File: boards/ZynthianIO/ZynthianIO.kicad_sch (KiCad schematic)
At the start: 25 parts, among them J1 Raspberry_Pi_2_3, J2 GPIO, U1 MCP23017_SP, U2 6N138, U3 74LS14

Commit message: Added IO Expander 3D model and connectors to case design, added references to sources.
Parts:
- Ctrl1, Ctrl2, Ctrl3, Ctrl4: footprint Connector_PinSocket_2.54mm:PinSocket_1x04_P2.54mm_Vertical -> Connector_PinHeader_2.54mm:PinHeader_1x04_P2.54mm_Vertical
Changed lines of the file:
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@@
       (effects (font (size 1.27 1.27)) (justify left))
     )
-    (property "Footprint" "Connector_PinSocket_2.54mm:PinSocket_1x04_P2.54mm_Vertical" (at 130.81 173.99 0)
+    (property "Footprint" "Connector_PinHeader_2.54mm:PinHeader_1x04_P2.54mm_Vertical" (at 130.81 173.99 0)
       (effects (font (size 1.27 1.27)) hide)
     )
@@
       (effects (font (size 1.27 1.27)) (justify left))
     )
-    (property "Footprint" "Connector_PinSocket_2.54mm:PinSocket_1x04_P2.54mm_Vertical" (at 130.81 158.75 0)
+    (property "Footprint" "Connector_PinHeader_2.54mm:PinHeader_1x04_P2.54mm_Vertical" (at 130.81 158.75 0)
       (effects (font (size 1.27 1.27)) hide)
     )
@@
       (effects (font (size 1.27 1.27)) (justify left))
     )
-    (property "Footprint" "Connector_PinSocket_2.54mm:PinSocket_1x04_P2.54mm_Vertical" (at 130.81 128.27 0)
+    (property "Footprint" "Connector_PinHeader_2.54mm:PinHeader_1x04_P2.54mm_Vertical" (at 130.81 128.27 0)
       (effects (font (size 1.27 1.27)) hide)
     )
@@
       (effects (font (size 1.27 1.27)) (justify left))
     )
-    (property "Footprint" "Connector_PinSocket_2.54mm:PinSocket_1x04_P2.54mm_Vertical" (at 130.81 143.51 0)
-      (effects (font (size 1.27 1.27)) hide)
-    )
+    (property "Footprint" "Connector_PinHeader_2.54mm:PinHeader_1x04_P2.54mm_Vertical" (at 130.81 143.51 0)
+      (effects (font (size 1.27 1.27)) hide)
+    )

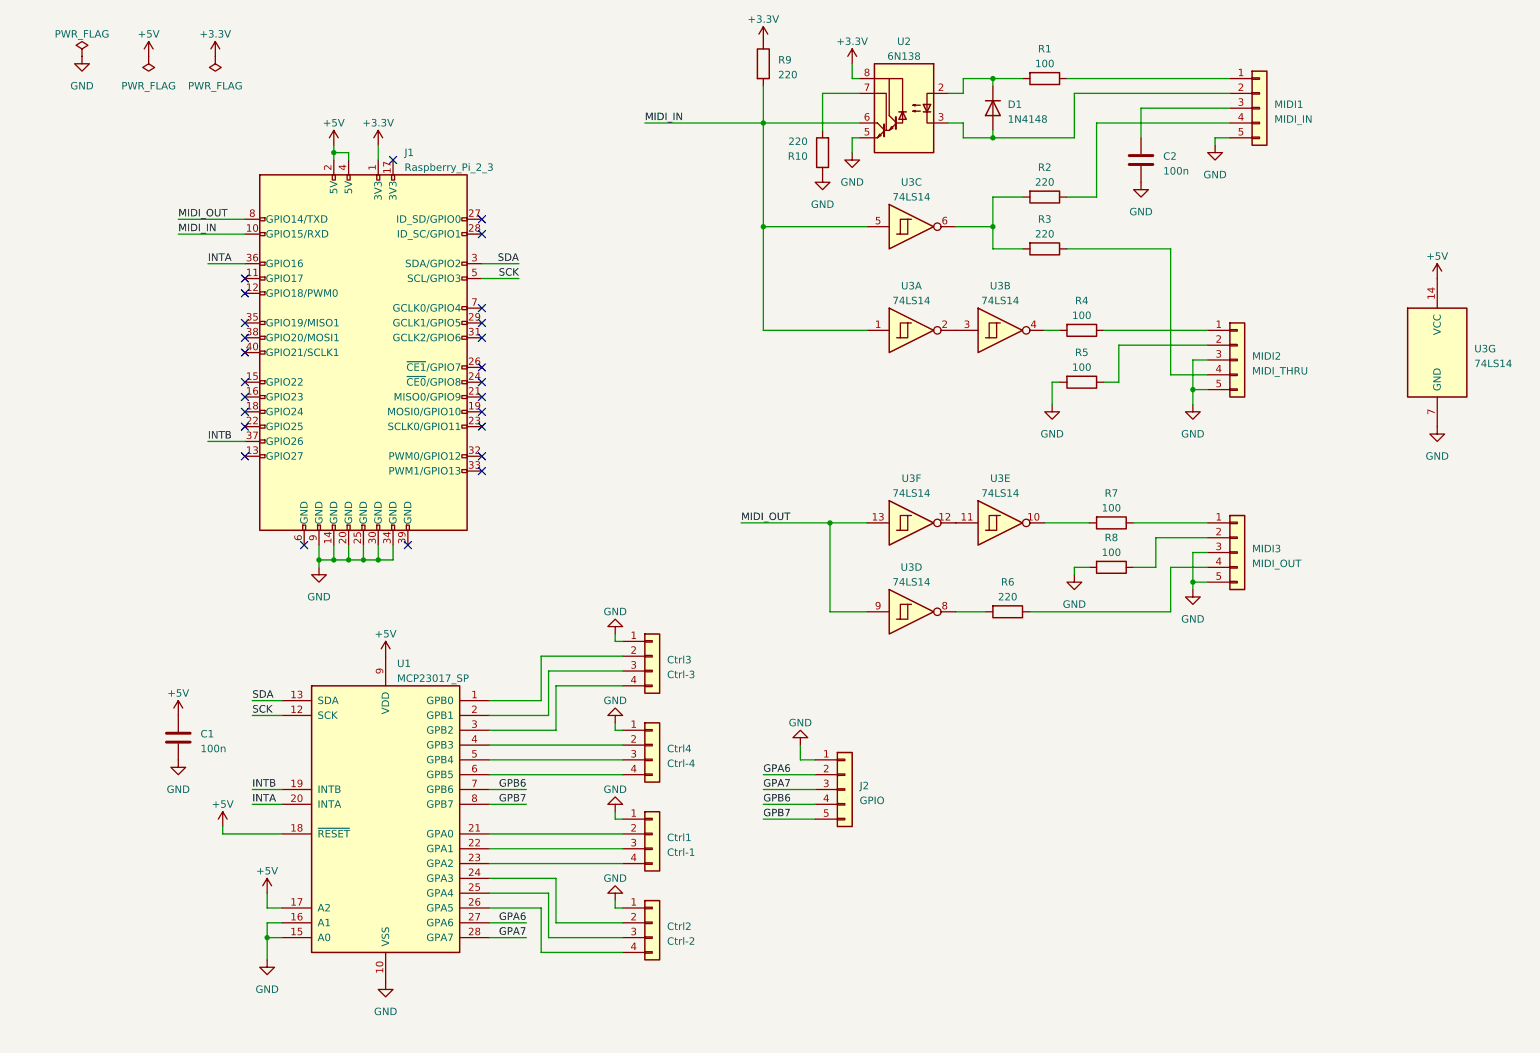
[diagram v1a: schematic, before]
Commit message: Updated IO expander board with Raspberry HAT template PCB design
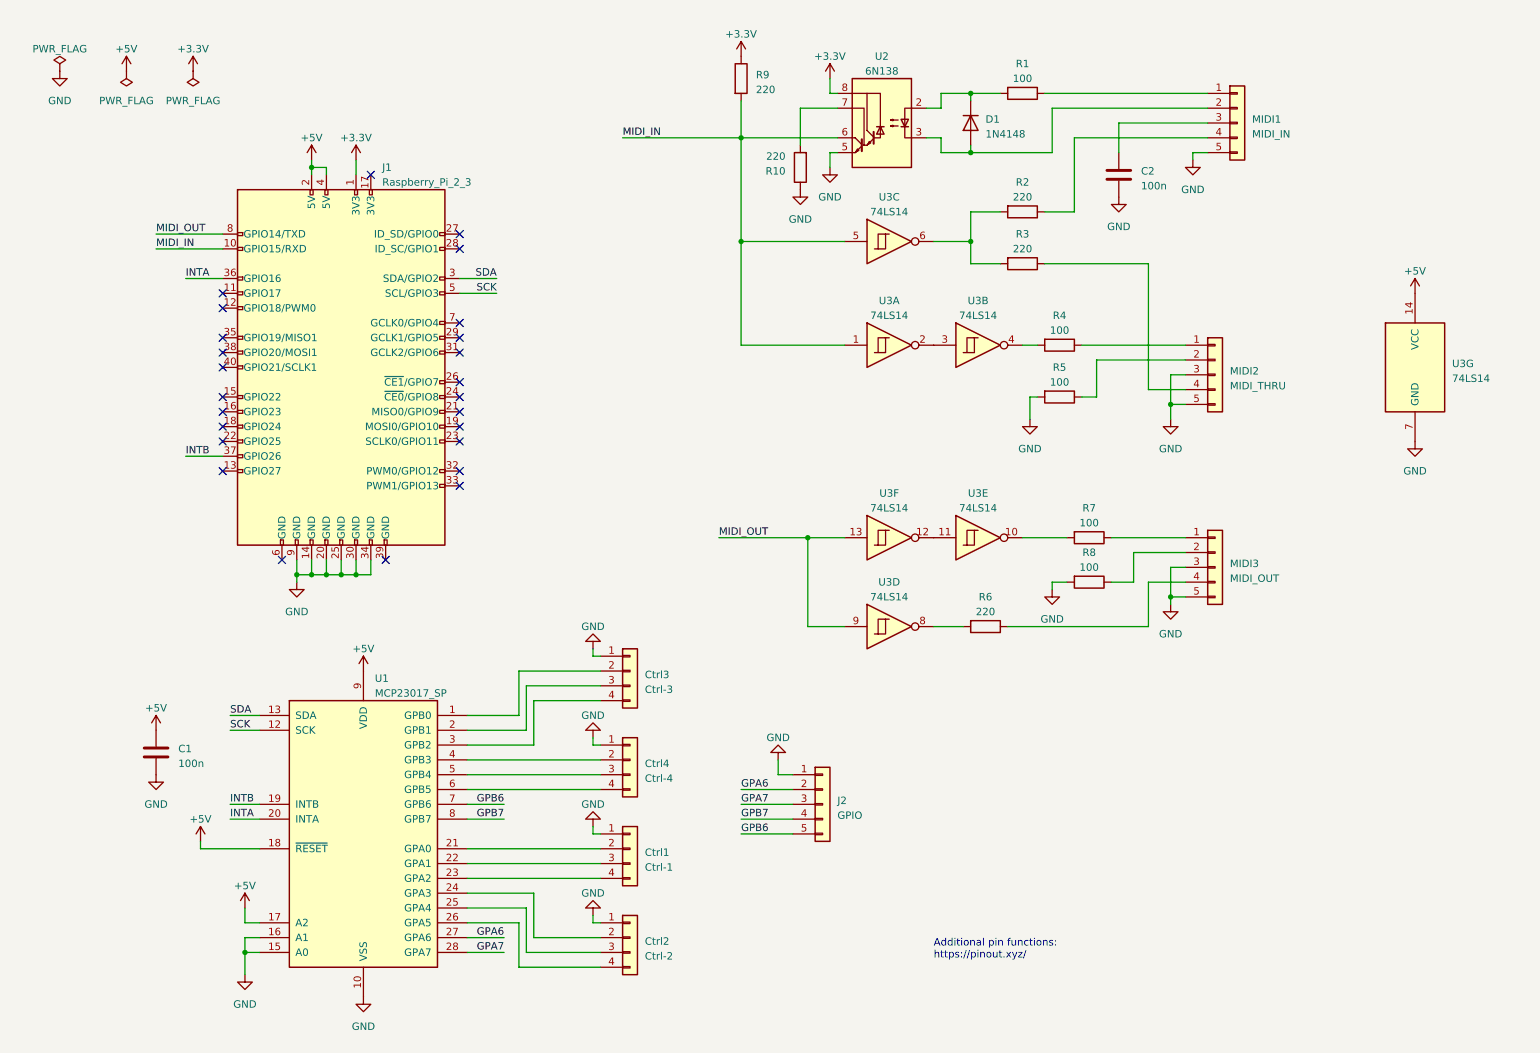
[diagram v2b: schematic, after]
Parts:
- R1, R10, R2, R3, R4, R5, R6, R7, R8, R9: footprint Resistor_THT:R_Axial_DIN0204_L3.6mm_D1.6mm_P5.08mm_Horizontal -> Resistor_THT:R_Axial_DIN0207_L6.3mm_D2.5mm_P7.62mm_Horizontal
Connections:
- net GPB6: now also J2.5 (Pin_5); no longer J2.4 (Pin_4)
- net GPB7: now also J2.4 (Pin_4); no longer J2.5 (Pin_5)
- net +3.3V renamed +3V3
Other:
- note added: "Additional pin functions: https://pinout.xyz/"

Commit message: Fixing several layout issues due to KiCAD 7.0.2/Linux update
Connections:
- net +3V3 renamed +3.3V

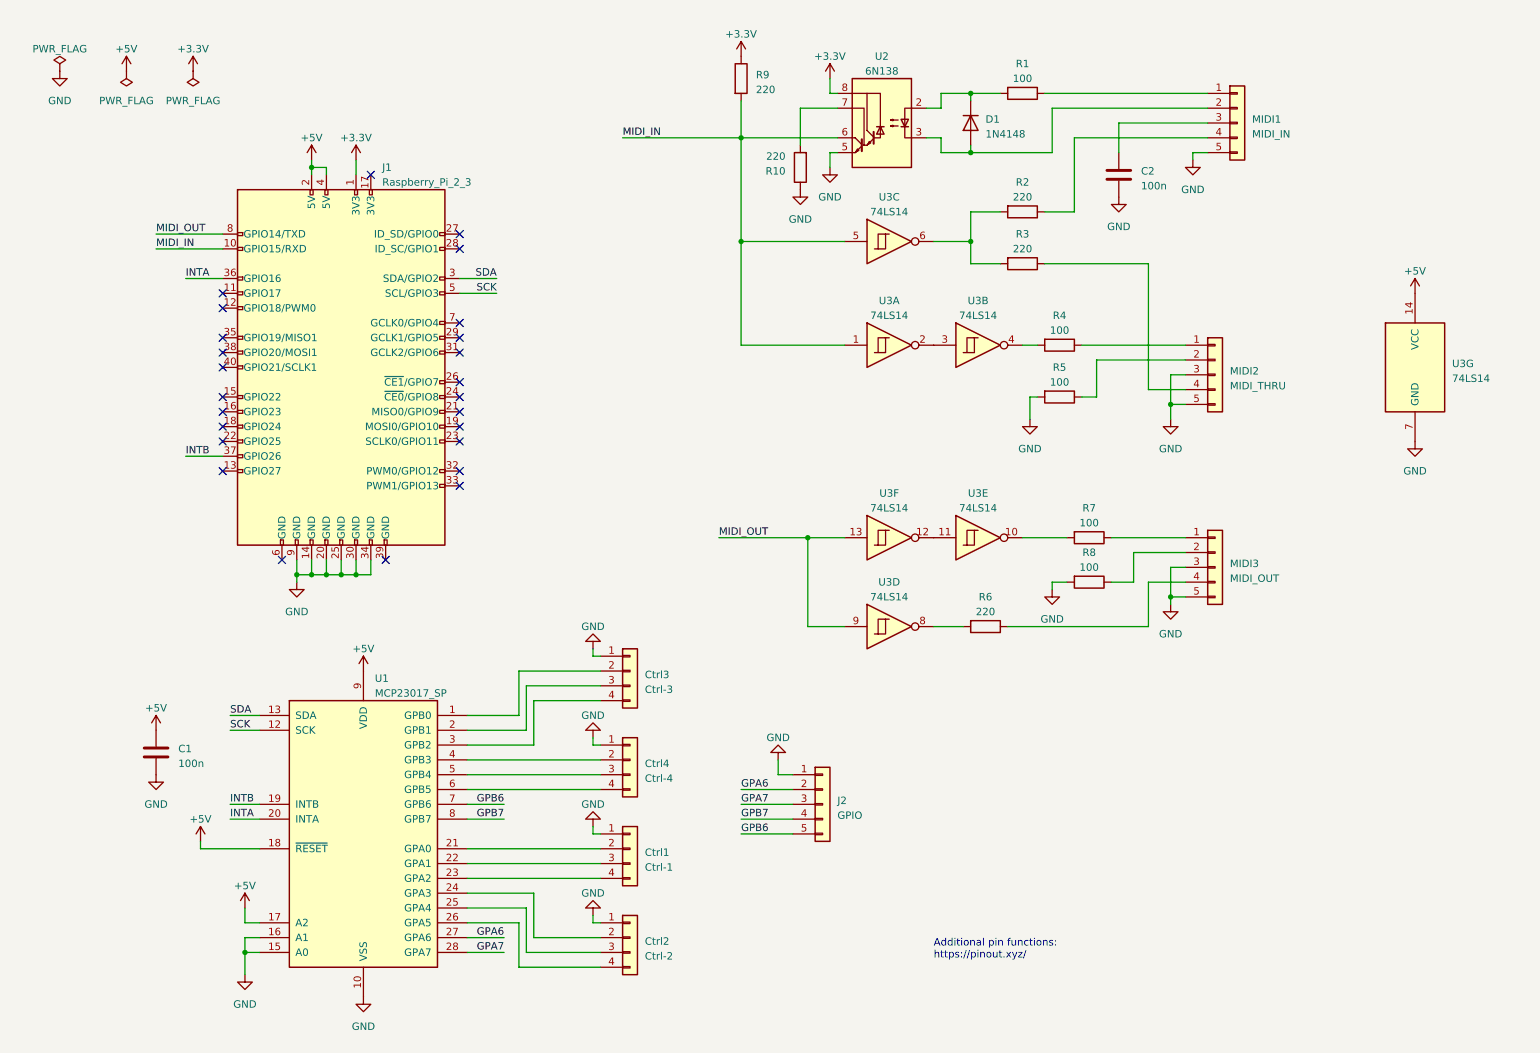
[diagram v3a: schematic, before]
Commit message: New ZynthianIO board design for Boutique case
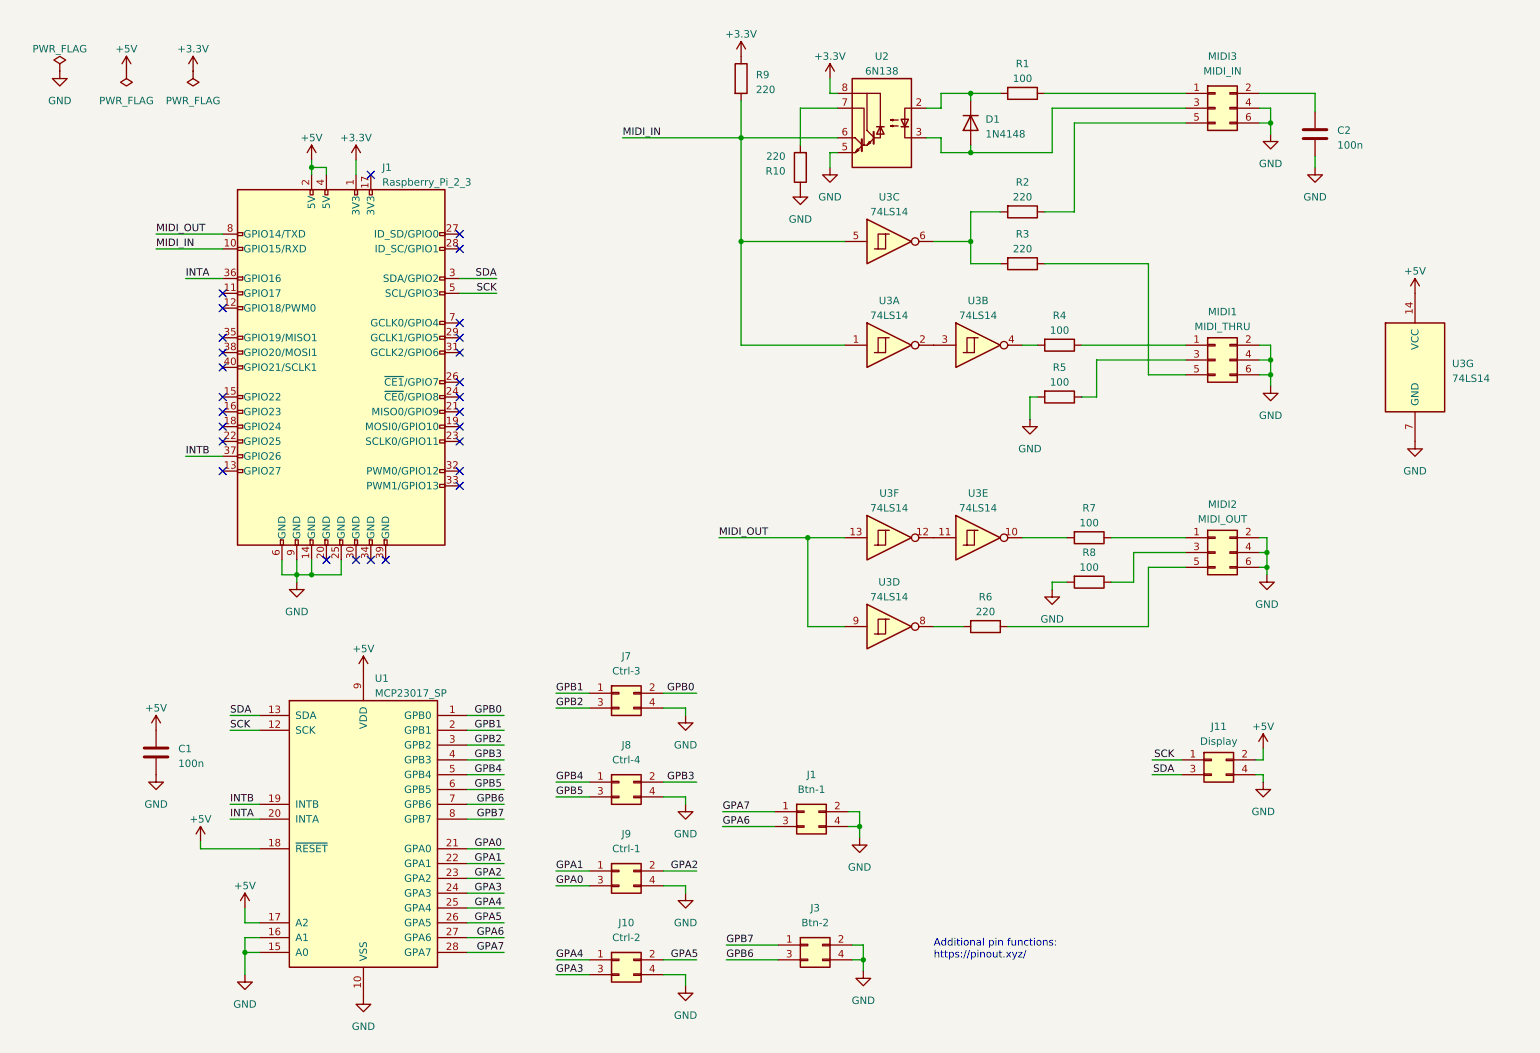
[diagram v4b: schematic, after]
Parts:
- removed Ctrl1: Ctrl-1, Connector_PinHeader_2.54mm:PinHeader_1x04_P2.54mm_Vertical, symbol Connector_Generic:Conn_01x04
- removed Ctrl2: Ctrl-2, Connector_PinHeader_2.54mm:PinHeader_1x04_P2.54mm_Vertical, symbol Connector_Generic:Conn_01x04
- removed Ctrl3: Ctrl-3, Connector_PinHeader_2.54mm:PinHeader_1x04_P2.54mm_Vertical, symbol Connector_Generic:Conn_01x04
- removed Ctrl4: Ctrl-4, Connector_PinHeader_2.54mm:PinHeader_1x04_P2.54mm_Vertical, symbol Connector_Generic:Conn_01x04
- removed J2: GPIO, Connector_PinHeader_2.54mm:PinHeader_1x05_P2.54mm_Vertical, symbol Connector_Generic:Conn_01x05
- removed MIDI1: MIDI_IN, Connector_JST:JST_EH_B5B-EH-A_1x05_P2.50mm_Vertical, symbol Connector_Generic:Conn_01x05
- removed MIDI2: MIDI_THRU, Connector_JST:JST_EH_B5B-EH-A_1x05_P2.50mm_Vertical, symbol Connector_Generic:Conn_01x05
- removed MIDI3: MIDI_OUT, Connector_JST:JST_EH_B5B-EH-A_1x05_P2.50mm_Vertical, symbol Connector_Generic:Conn_01x05
- added J1: Btn-1, Connector_PinHeader_2.54mm:PinHeader_2x02_P2.54mm_Horizontal, symbol Connector_Generic:Conn_02x02_Odd_Even
- added J10: Ctrl-2, Connector_PinHeader_2.54mm:PinHeader_2x02_P2.54mm_Horizontal, symbol Connector_Generic:Conn_02x02_Odd_Even
- added J11: Display, Connector_PinHeader_2.54mm:PinHeader_2x02_P2.54mm_Horizontal, symbol Connector_Generic:Conn_02x02_Odd_Even
- added J3: Btn-2, Connector_PinHeader_2.54mm:PinHeader_2x02_P2.54mm_Horizontal, symbol Connector_Generic:Conn_02x02_Odd_Even
- added J7: Ctrl-3, Connector_PinHeader_2.54mm:PinHeader_2x02_P2.54mm_Horizontal, symbol Connector_Generic:Conn_02x02_Odd_Even
- added J8: Ctrl-4, Connector_PinHeader_2.54mm:PinHeader_2x02_P2.54mm_Horizontal, symbol Connector_Generic:Conn_02x02_Odd_Even
- added J9: Ctrl-1, Connector_PinHeader_2.54mm:PinHeader_2x02_P2.54mm_Horizontal, symbol Connector_Generic:Conn_02x02_Odd_Even
- added MIDI1: MIDI_THRU, Connector_PinHeader_2.54mm:PinHeader_2x03_P2.54mm_Horizontal, symbol Connector_Generic:Conn_02x03_Odd_Even
- added MIDI2: MIDI_OUT, Connector_PinHeader_2.54mm:PinHeader_2x03_P2.54mm_Horizontal, symbol Connector_Generic:Conn_02x03_Odd_Even
- added MIDI3: MIDI_IN, Connector_PinHeader_2.54mm:PinHeader_2x03_P2.54mm_Horizontal, symbol Connector_Generic:Conn_02x03_Odd_Even
- D1: footprint Diode_THT:D_DO-35_SOD27_P2.54mm_Vertical_AnodeUp -> Diode_THT:D_DO-34_SOD68_P7.62mm_Horizontal
- J1: footprint Connector_PinHeader_2.54mm:PinHeader_2x20_P2.54mm_Vertical -> Connector_PinSocket_2.54mm:PinSocket_2x20_P2.54mm_Vertical
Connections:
- net +5V: now also J11.2 (Pin_2)
- net GND: now also J1.6 (GND), J1.2 (Pin_2), J1.4 (Pin_4), J10.4 (Pin_4), J11.4 (Pin_4), J3.2 (Pin_2), J3.4 (Pin_4), J7.4 (Pin_4), J8.4 (Pin_4), J9.4 (Pin_4), MIDI1.2 (Pin_2), MIDI1.4 (Pin_4), MIDI1.6 (Pin_6), MIDI2.2 (Pin_2), MIDI2.4 (Pin_4), MIDI2.6 (Pin_6), MIDI3.4 (Pin_4), MIDI3.6 (Pin_6); no longer J1.20 (GND), J1.30 (GND), J1.34 (GND)
- net GPA6: now also J1.3 (Pin_3)
- net GPA7: now also J1.1 (Pin_1)
- net GPB6: now also J3.3 (Pin_3)
- net GPB7: now also J3.1 (Pin_1)
- net SCK: now also J11.1 (Pin_1)
- net SDA: now also J11.3 (Pin_3)
- net at R3.1: now also MIDI1.5 (Pin_5)
- net at R5.1: now also MIDI1.3 (Pin_3)
- net at D1.2 (A), U2.3 (C2): now also MIDI3.3 (Pin_3)
- net at R7.1: now also MIDI2.1 (Pin_1)
- net at R8.1: now also MIDI2.3 (Pin_3)
- net at R1.1: now also MIDI3.1 (Pin_1)
- net GPB0: now reaches U1.1 (GPB0)
- net GPB0: now also J7.2 (Pin_2)
- net GPB1: now reaches U1.2 (GPB1)
- net GPB1: now also J7.1 (Pin_1)
- net GPB2: now reaches U1.3 (GPB2)
- net GPB2: now also J7.3 (Pin_3)
- net GPB3: now reaches U1.4 (GPB3)
- net GPB3: now also J8.2 (Pin_2)
- net GPB4: now reaches U1.5 (GPB4)
- net GPB4: now also J8.1 (Pin_1)
- net GPB5: now reaches U1.6 (GPB5)
- net GPB5: now also J8.3 (Pin_3)
- net at R4.1: now also MIDI1.1 (Pin_1)
- net at R2.1: now also MIDI3.5 (Pin_5)
- net at R6.1: now also MIDI2.5 (Pin_5)
- net at C2.1: now also MIDI3.2 (Pin_2)
- net GPA0: now reaches U1.21 (GPA0)
- net GPA0: now also J9.3 (Pin_3)
- net GPA1: now reaches U1.22 (GPA1)
- net GPA1: now also J9.1 (Pin_1)
- net GPA2: now reaches U1.23 (GPA2)
- net GPA2: now also J9.2 (Pin_2)
- net GPA3: now reaches U1.24 (GPA3)
- net GPA3: now also J10.3 (Pin_3)
- net GPA4: now reaches U1.25 (GPA4)
- net GPA4: now also J10.1 (Pin_1)
- net GPA5: now reaches U1.26 (GPA5)
- net GPA5: now also J10.2 (Pin_2)
- no-connect marks 25 -> 27
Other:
- moved on the sheet: C2

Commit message: Fixed MIDI interfaces
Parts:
- removed R10: 220, Resistor_THT:R_Axial_DIN0207_L6.3mm_D2.5mm_P7.62mm_Horizontal, symbol Device:R
- D1: footprint Diode_THT:D_DO-34_SOD68_P7.62mm_Horizontal -> Diode_THT:D_DO-35_SOD27_P7.62mm_Horizontal
- R1, R4, R5, R7, R8: value 100 -> 220
- R9: value 220 -> 2k2
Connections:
- net +5V: now also R4.2, R7.2
- net GND: no longer R5.2, R8.2
- net at U3.4: now also R5.2; no longer R4.2
- net at U3.10: now also R8.2; no longer R7.2
- no-connect marks 27 -> 28
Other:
- moved on the sheet: MIDI1, MIDI2, R4, R5, R6, R7, R8, R9, U3A, U3B, U3D, U3E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
